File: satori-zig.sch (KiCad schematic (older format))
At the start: 2 parts, among them CN1 DF12-3.5-20DP, CN2 CONN_01X06

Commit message: Input Net name
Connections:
- net RX: now reaches CN1.17, CN2.4 (P4)
- net TX: now reaches CN1.19, CN2.5 (P5)
- net WAKE: now reaches CN1.20, CN2.6 (P6)
- net RESET: now reaches CN1.3, CN2.3 (P3)
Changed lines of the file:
@@
 Wire Wire Line
 	6350 1200 6350 1300
+Text Label 3200 2600 0    60   ~ 0
+3V3
+Text Label 3200 2700 0    60   ~ 0
+GND
+Text Label 3200 2800 0    60   ~ 0
+RESET
+Text Label 3200 2900 0    60   ~ 0
+RX
+Text Label 3200 3000 0    60   ~ 0
+TX
+Text Label 3200 3100 0    60   ~ 0
+WAKE
 $EndSCHEMATC

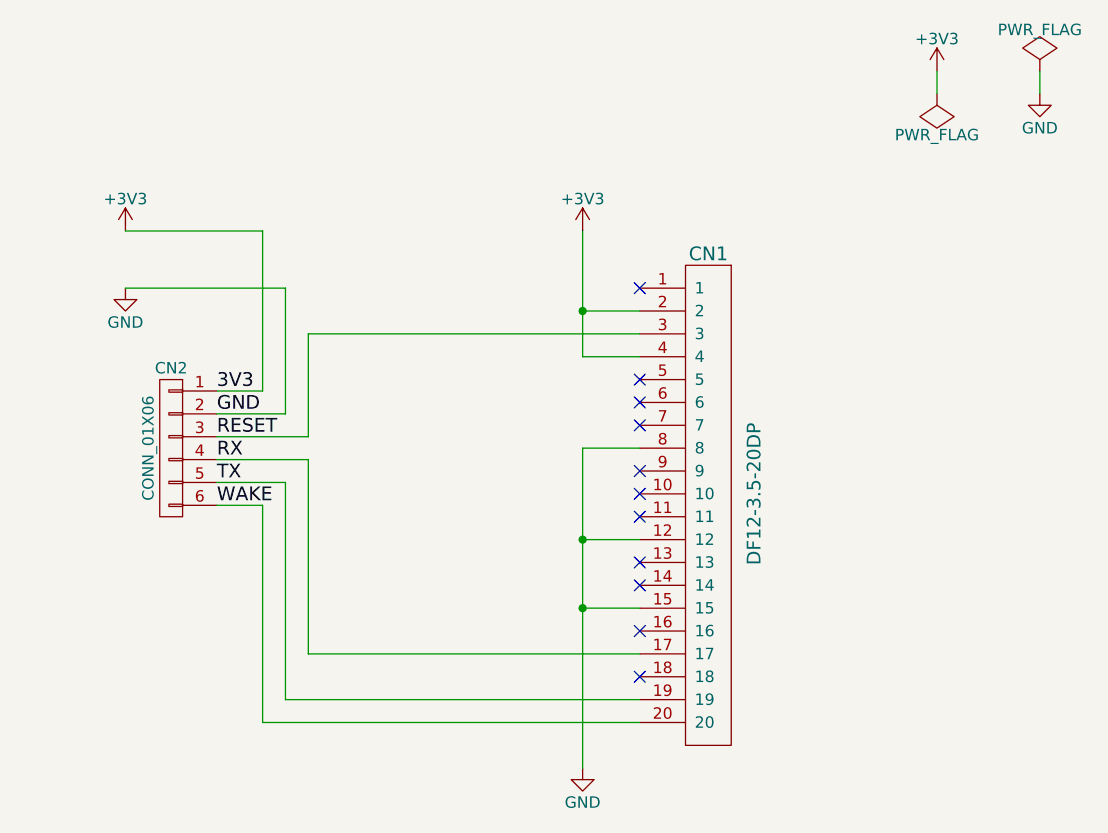
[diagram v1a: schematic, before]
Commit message: Remove hatching
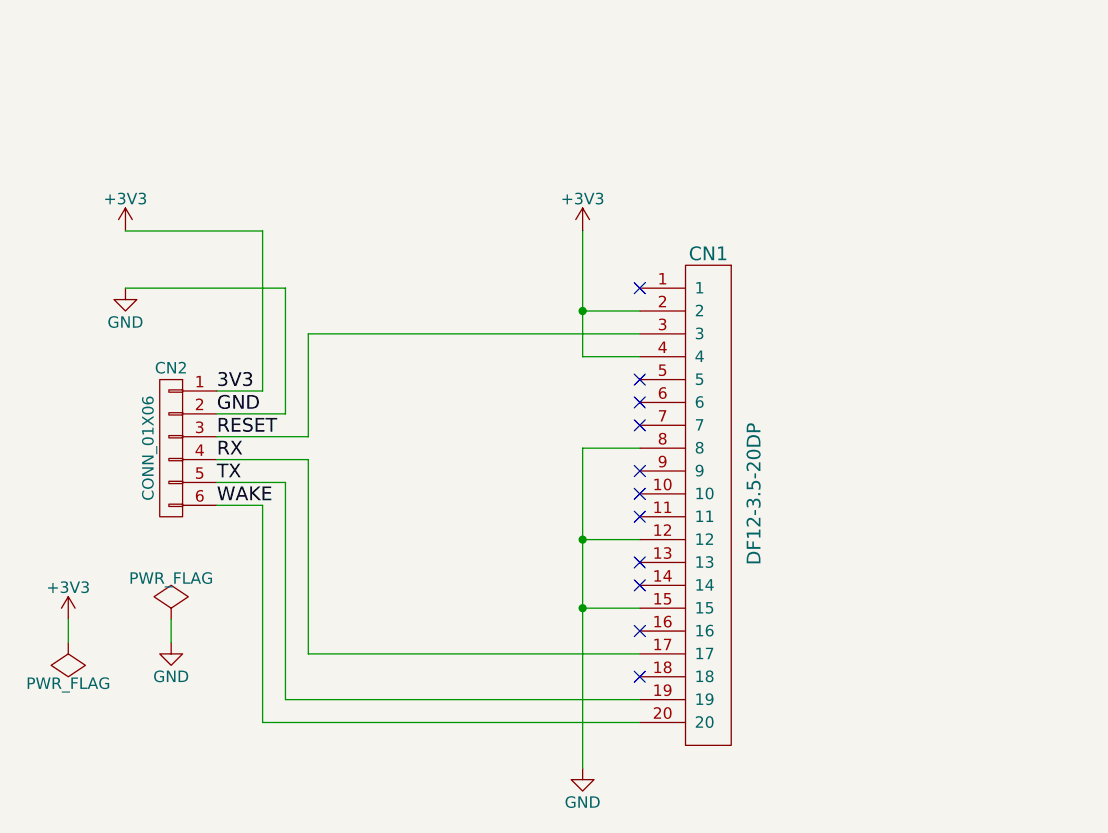
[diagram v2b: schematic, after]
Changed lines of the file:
@@
 L PWR_FLAG #FLG1
 U 1 1 584FB311
-P 6350 1300
-F 0 "#FLG1" H 6350 1395 50  0001 C CNN
-F 1 "PWR_FLAG" H 6350 1480 50  0000 C CNN
-F 2 "" H 6350 1300 50  0000 C CNN
-F 3 "" H 6350 1300 50  0000 C CNN
-	1    6350 1300
+P 2550 3700
+F 0 "#FLG1" H 2550 3795 50  0001 C CNN
+F 1 "PWR_FLAG" H 2550 3880 50  0000 C CNN
+F 2 "" H 2550 3700 50  0000 C CNN
+F 3 "" H 2550 3700 50  0000 C CNN
+	1    2550 3700
 	1    0    0    1
 $EndComp
@@
 L PWR_FLAG #FLG2
 U 1 1 584FB32B
-P 6800 1200
-F 0 "#FLG2" H 6800 1295 50  0001 C CNN
-F 1 "PWR_FLAG" H 6800 1380 50  0000 C CNN
-F 2 "" H 6800 1200 50  0000 C CNN
-F 3 "" H 6800 1200 50  0000 C CNN
-	1    6800 1200
+P 3000 3600
+F 0 "#FLG2" H 3000 3695 50  0001 C CNN
+F 1 "PWR_FLAG" H 3000 3780 50  0000 C CNN
+F 2 "" H 3000 3600 50  0000 C CNN
+F 3 "" H 3000 3600 50  0000 C CNN
+	1    3000 3600
 	1    0    0    -1
 $EndComp
@@
 L +3V3 #PWR5
 U 1 1 584FB347
-P 6350 1200
-F 0 "#PWR5" H 6350 1050 50  0001 C CNN
-F 1 "+3V3" H 6350 1340 50  0000 C CNN
-F 2 "" H 6350 1200 50  0000 C CNN
-F 3 "" H 6350 1200 50  0000 C CNN
-	1    6350 1200
+P 2550 3600
+F 0 "#PWR5" H 2550 3450 50  0001 C CNN
+F 1 "+3V3" H 2550 3740 50  0000 C CNN
+F 2 "" H 2550 3600 50  0000 C CNN
+F 3 "" H 2550 3600 50  0000 C CNN
+	1    2550 3600
 	1    0    0    -1
 $EndComp
@@
 L GND #PWR6
 U 1 1 584FB361
-P 6800 1300
-F 0 "#PWR6" H 6800 1050 50  0001 C CNN
-F 1 "GND" H 6800 1150 50  0000 C CNN
-F 2 "" H 6800 1300 50  0000 C CNN
-F 3 "" H 6800 1300 50  0000 C CNN
-	1    6800 1300
+P 3000 3700
+F 0 "#PWR6" H 3000 3450 50  0001 C CNN
+F 1 "GND" H 3000 3550 50  0000 C CNN
+F 2 "" H 3000 3700 50  0000 C CNN
+F 3 "" H 3000 3700 50  0000 C CNN
+	1    3000 3700
 	1    0    0    -1
 $EndComp
 Wire Wire Line
-	6800 1200 6800 1300
+	3000 3600 3000 3700
 Wire Wire Line
-	6350 1200 6350 1300
+	2550 3600 2550 3700
 Text Label 3200 2600 0    60   ~ 0
 3V3
